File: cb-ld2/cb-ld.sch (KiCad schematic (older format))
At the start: 22 parts, among them P1 CONN_01X14, P2 CONN_01X14, U1 SKY13385, U2 MGA-81563, U3 MBC13916, U4 SKY13385

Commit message: Setting values for 433 MHz
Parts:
- removed C4: 3p, mysmd:SM0603S, symbol C
- added R?: 24, symbol R
- C3: value 10n -> 100n
- C5: value 1.5p -> 2.4p
- L2: value 10n -> 33n
- L3: value 10n -> 1u
- L4: value 6.8n -> 39n
- PS1: symbol PANSTAMP_NRG2 -> PANSTAMP_NRG2-RESCUE-cb-ld
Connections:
- wire segments 137 -> 136
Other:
- moved on the sheet: C5
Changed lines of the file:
@@
 EESchema Schematic File Version 2
+LIBS:cb-ld-rescue
 LIBS:power
 LIBS:device
@@
 encoding utf-8
 Sheet 1 1
-Title "cb-ld2"
+Title "cb-ld2 for 433 MHz applications"
 Date "2016-03-04"
 Rev "0.1"
@@
 $EndComp
 $Comp
-L PANSTAMP_NRG2 PS1
+L PANSTAMP_NRG2-RESCUE-cb-ld PS1
 U 1 1 54EE0213
 P 4850 4550
@@
 L C C5
 U 1 1 56D9BAD5
-P 9300 6250
-F 0 "C5" H 9350 6350 50  0000 L CNN
-F 1 "1.5p" H 9350 6150 50  0000 L CNN
-F 2 "mysmd:SM0603S" H 9300 6250 60  0001 C CNN
-F 3 "" H 9300 6250 60  0001 C CNN
-	1    9300 6250
+P 8900 6250
+F 0 "C5" H 8950 6350 50  0000 L CNN
+F 1 "2.4p" H 8950 6150 50  0000 L CNN
+F 2 "mysmd:SM0603S" H 8900 6250 60  0001 C CNN
+F 3 "" H 8900 6250 60  0001 C CNN
+	1    8900 6250
 	0    1    1    0
 $EndComp
-$Comp
-L C C4
-U 1 1 56D9BADC
-P 9050 6450
-F 0 "C4" H 9100 6550 50  0000 L CNN
-F 1 "3p" H 9100 6350 50  0000 L CNN
-F 2 "mysmd:SM0603S" H 9050 6450 60  0001 C CNN
-F 3 "" H 9050 6450 60  0001 C CNN
-	1    9050 6450
-	-1   0    0    1
-$EndComp
-Wire Wire Line
-	7700 6250 9150 6250
-Wire Wire Line
-	9050 6300 9050 6250
-Connection ~ 9050 6250
-$Comp
-L GND #PWR07
-U 1 1 56D9BAE6
-P 9050 6650
-F 0 "#PWR07" H 9050 6650 30  0001 C CNN
-F 1 "GND" H 9050 6580 30  0001 C CNN
-F 2 "" H 9050 6650 60  0001 C CNN
-F 3 "" H 9050 6650 60  0001 C CNN
-	1    9050 6650
-	-1   0    0    -1
-$EndComp
-Wire Wire Line
-	9050 6600 9050 6650
 $Comp
 L INDUCTOR_SMALL L2
@@
 P 9550 5800
 F 0 "L2" V 9504 5878 50  0000 L CNN
-F 1 "10n" V 9596 5878 50  0000 L CNN
+F 1 "33n" V 9596 5878 50  0000 L CNN
 F 2 "mysmd:SM0603S" H 9550 5800 50  0001 C CNN
 F 3 "" H 9550 5800 50  0000 C CNN
@@
 P 9050 5750
 F 0 "C3" H 9100 5850 50  0000 L CNN
-F 1 "10n" H 9100 5650 50  0000 L CNN
+F 1 "100n" H 9100 5650 50  0000 L CNN
 F 2 "mysmd:SM0603S" H 9050 5750 60  0001 C CNN
 F 3 "" H 9050 5750 60  0001 C CNN
@@
 P 11000 6250
 F 0 "L4" H 11000 6466 50  0000 C CNN
-F 1 "6.8n" H 11000 6374 50  0000 C CNN
+F 1 "39n" H 11000 6374 50  0000 C CNN
 F 2 "mysmd:SM0603S" H 11000 6250 50  0001 C CNN
 F 3 "" H 11000 6250 50  0000 C CNN
@@
 P 10350 3350
 F 0 "L3" V 10300 3200 50  0000 L CNN
-F 1 "10n" V 10400 3150 50  0000 L CNN
+F 1 "1u" V 10400 3150 50  0000 L CNN
 F 2 "mysmd:SM0603S" H 10350 3350 50  0001 C CNN
 F 3 "" H 10350 3350 50  0000 C CNN
@@
 Text Label 7050 6200 2    60   ~ 0
 RX_LNA
+$Comp
+L R R?
+U 1 1 57024CE4
+P 9300 6250
+F 0 "R?" V 9200 6250 50  0000 C CNN
+F 1 "24" V 9300 6250 50  0000 C CNN
+F 2 "" V 9230 6250 50  0000 C CNN
+F 3 "" H 9300 6250 50  0000 C CNN
+	1    9300 6250
+	0    1    1    0
+$EndComp
+Wire Wire Line
+	9150 6250 9050 6250
+Wire Wire Line
+	7700 6250 8750 6250
 $EndSCHEMATC

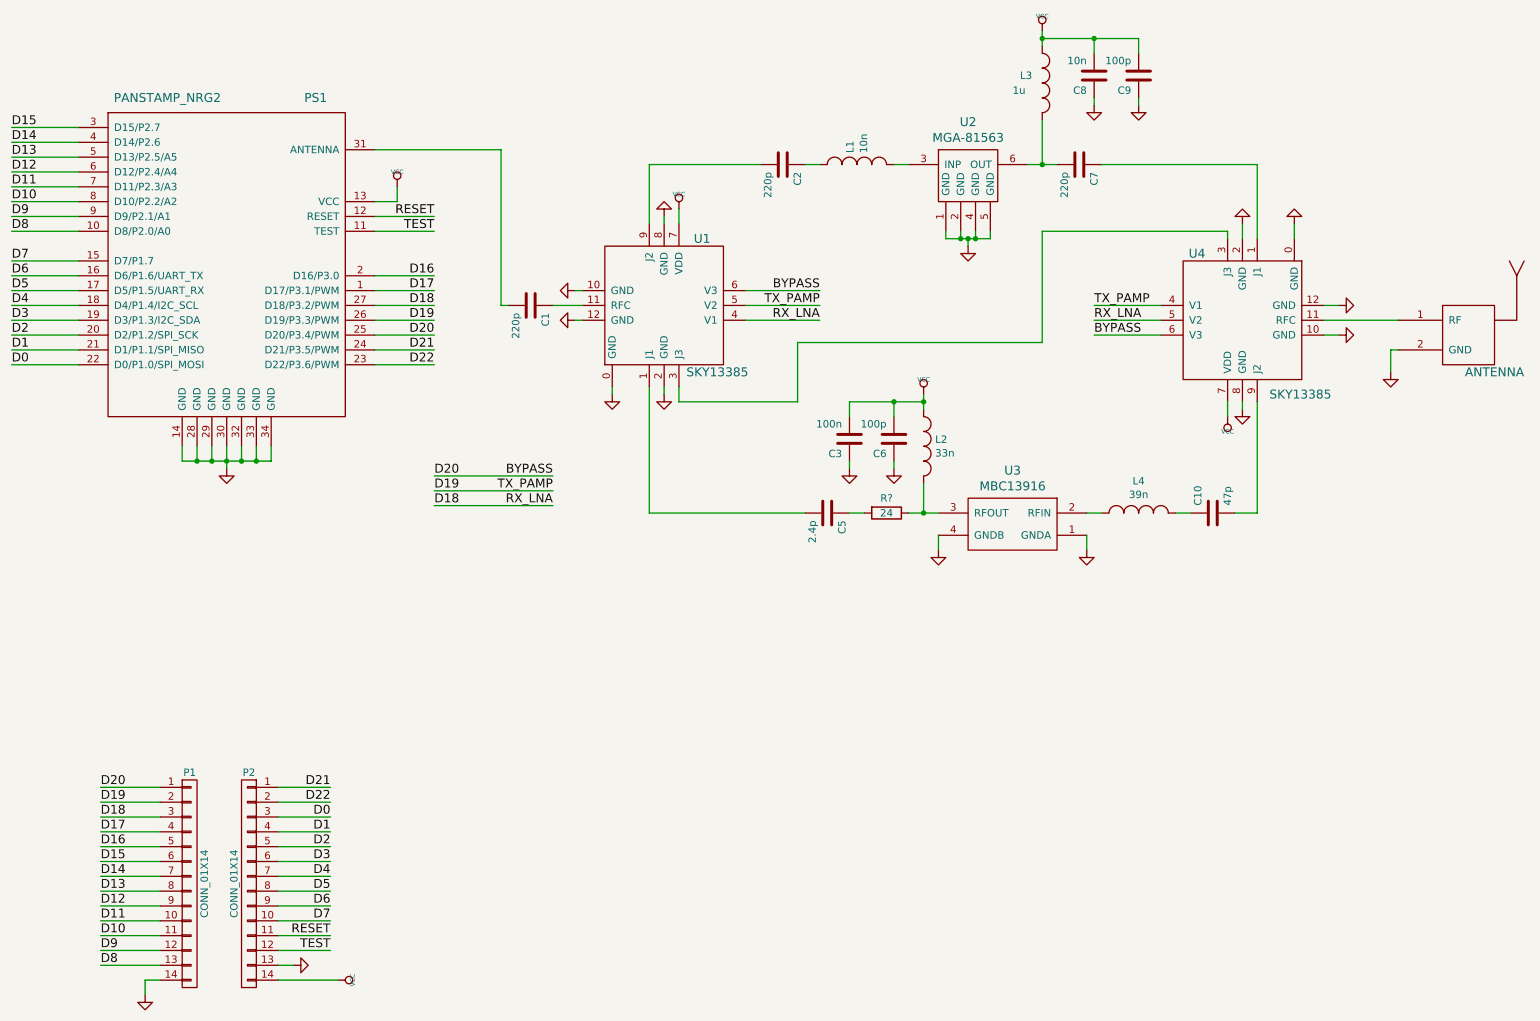
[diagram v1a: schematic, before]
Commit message: Natural evolution of the design after doing some tests
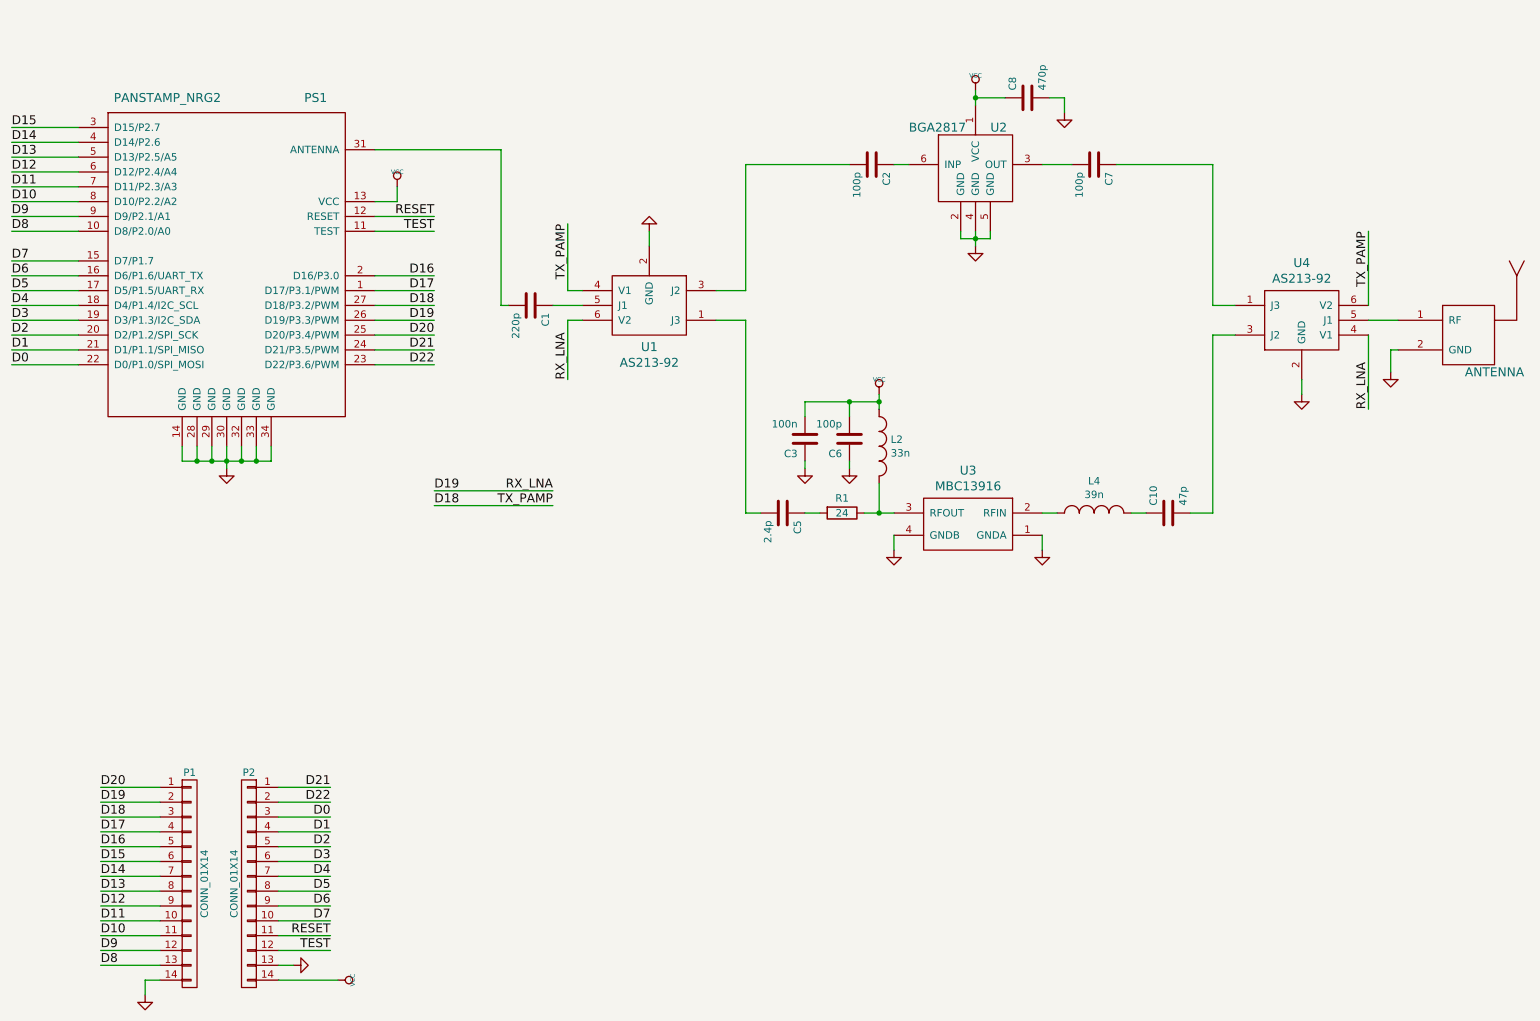
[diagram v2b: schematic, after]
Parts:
- removed C9: 100p, mysmd:SM0603S, symbol C
- removed L1: 10n, mysmd:SM0603S, symbol INDUCTOR_SMALL
- removed L3: 1u, mysmd:SM0603S, symbol INDUCTOR_SMALL
- removed U1, U4: SKY13385, mysmd:QFN12, symbol SKY13385
- removed U2: MGA-81563, mysmd:SC-70, symbol MGA-81563
- added U1, U4: AS213-92, mysmd:SC-70, symbol AS213-92
- added U2: BGA2817, mysmd:SC-70, symbol BGA2817
- C2, C7: value 220p -> 100p
- C8: value 10n -> 470p
- R1: renamed from R?; footprint (none) -> mysmd:SM0603S
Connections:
- net D18: now also U1.4 (V1), U4.6 (V2)
- net D19: now also U1.6 (V2), U4.4 (V1)
- net GND: now also C8.2, U1.2 (GND), U2.2 (GND), U2.4 (GND), U2.5 (GND), U4.2 (GND); no longer C8.1
- net VCC: now also C8.1, U2.1 (VCC); no longer C8.2
- net at ANT1.1 (RF): now also U4.5 (J1)
- net at C5.2: now also U1.1 (J3)
- net at C10.2: now also U4.3 (J2)
- net at C1.1: now also U1.5 (J1)
- net at C2.2: now also U1.3 (J2)
- net at C7.1: now also U4.1 (J3)
- net at C7.2: now also U2.3 (OUT)
- net at C2.1: now also U2.6 (INP)
- net BYPASS renamed D20
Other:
- moved on the sheet: C10, C2, C3, C5, C6, C7, C8, L2, L4, R1, U3

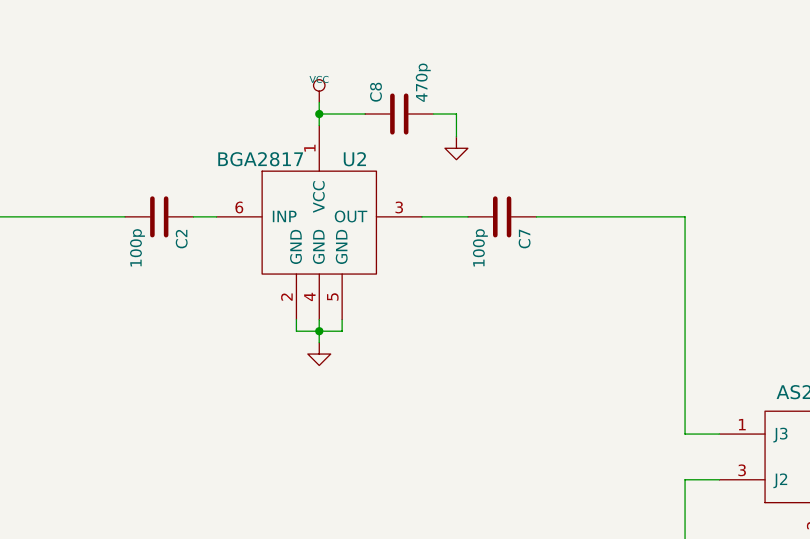
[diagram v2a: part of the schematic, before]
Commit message: PA replaced by MGA82563
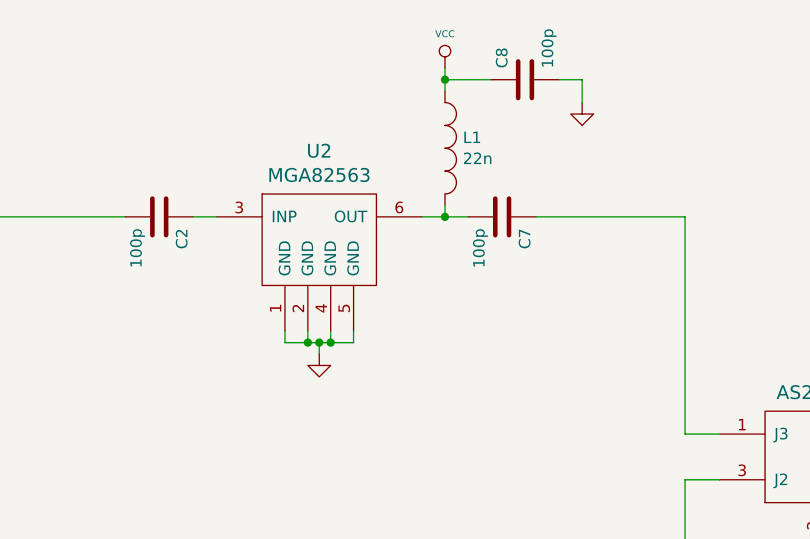
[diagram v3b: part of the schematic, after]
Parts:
- removed U2: BGA2817, mysmd:SC-70, symbol BGA2817
- added L1: 22n, mysmd:SM0603S, symbol INDUCTOR_SMALL
- added U2: MGA82563, mysmd:SC-70, symbol MGA82563
- C8: value 470p -> 100p
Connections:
- net GND: now also U2.1 (GND), U2.2 (GND), U2.4 (GND), U2.5 (GND)
- net VCC: now also L1.1
- net at C2.1: now also U2.3 (INP)
- net at C7.2: now also L1.2, U2.6 (OUT)
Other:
- moved on the sheet: C8
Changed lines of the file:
@@
 Title "cb-ld2 for 433 MHz applications"
 Date "2016-05-06"
-Rev "0.1"
+Rev "0.2"
 Comp "panStamp"
 Comment1 ""
@@
 L GND #PWR013
 U 1 1 56DA560D
-P 9900 4450
-F 0 "#PWR013" H 9900 4450 30  0001 C CNN
-F 1 "GND" H 9900 4380 30  0001 C CNN
-F 2 "" H 9900 4450 60  0001 C CNN
-F 3 "" H 9900 4450 60  0001 C CNN
-	1    9900 4450
-	1    0    0    -1
-$EndComp
-Wire Wire Line
-	9900 4350 9900 4450
-Connection ~ 9900 4400
-Wire Wire Line
-	9800 4350 9800 4400
+P 9900 4500
+F 0 "#PWR013" H 9900 4500 30  0001 C CNN
+F 1 "GND" H 9900 4430 30  0001 C CNN
+F 2 "" H 9900 4500 60  0001 C CNN
+F 3 "" H 9900 4500 60  0001 C CNN
+	1    9900 4500
+	1    0    0    -1
+$EndComp
 $Comp
 L C C7
@@
 L VCC #PWR014
 U 1 1 56DA5DCA
-P 9900 3400
-F 0 "#PWR014" H 9900 3500 30  0001 C CNN
-F 1 "VCC" H 9900 3500 30  0000 C CNN
-F 2 "" H 9900 3400 60  0001 C CNN
-F 3 "" H 9900 3400 60  0001 C CNN
-	1    9900 3400
+P 10450 3250
+F 0 "#PWR014" H 10450 3350 30  0001 C CNN
+F 1 "VCC" H 10450 3400 30  0000 C CNN
+F 2 "" H 10450 3250 60  0001 C CNN
+F 3 "" H 10450 3250 60  0001 C CNN
+	1    10450 3250
 	1    0    0    -1
 $EndComp
@@
 L C C8
 U 1 1 56DA6253
-P 10250 3450
-F 0 "C8" H 10300 3550 50  0000 L CNN
-F 1 "470p" H 10300 3350 50  0000 L CNN
-F 2 "mysmd:SM0603S" H 10250 3450 60  0001 C CNN
-F 3 "" H 10250 3450 60  0001 C CNN
-	1    10250 3450
+P 10800 3300
+F 0 "C8" H 10850 3400 50  0000 L CNN
+F 1 "100p" H 10850 3200 50  0000 L CNN
+F 2 "mysmd:SM0603S" H 10800 3300 60  0001 C CNN
+F 3 "" H 10800 3300 60  0001 C CNN
+	1    10800 3300
 	0    -1   -1   0
 $EndComp
@@
 L GND #PWR015
 U 1 1 56DA6263
-P 10500 3550
-F 0 "#PWR015" H 10500 3550 30  0001 C CNN
-F 1 "GND" H 10500 3480 30  0001 C CNN
-F 2 "" H 10500 3550 60  0001 C CNN
-F 3 "" H 10500 3550 60  0001 C CNN
-	1    10500 3550
+P 11050 3400
+F 0 "#PWR015" H 11050 3400 30  0001 C CNN
+F 1 "GND" H 11050 3330 30  0001 C CNN
+F 2 "" H 11050 3400 60  0001 C CNN
+F 3 "" H 11050 3400 60  0001 C CNN
+	1    11050 3400
 	-1   0    0    -1
 $EndComp
@@
 Wire Wire Line
 	12100 5450 12100 5350
-$Comp
-L BGA2817 U2
-U 1 1 572C5F7F
-P 9850 3950
-F 0 "U2" H 10000 4250 60  0000 L CNN
-F 1 "BGA2817" H 9450 4250 60  0000 L CNN
-F 2 "mysmd:SC-70" H 10000 4400 60  0001 C CNN
-F 3 "" H 10000 4400 60  0000 C CNN
-	1    9850 3950
-	1    0    0    -1
-$EndComp
 Wire Wire Line
 	11500 3900 10850 3900
 Wire Wire Line
-	9800 4400 10000 4400
-Wire Wire Line
-	10000 4400 10000 4350
-Wire Wire Line
 	10550 3900 10350 3900
 Wire Wire Line
-	9900 3400 9900 3500
-Wire Wire Line
-	10100 3450 9900 3450
-Connection ~ 9900 3450
-Wire Wire Line
-	10400 3450 10500 3450
-Wire Wire Line
-	10500 3450 10500 3550
+	10450 3250 10450 3350
+Wire Wire Line
+	10650 3300 10450 3300
+Connection ~ 10450 3300
+Wire Wire Line
+	10950 3300 11050 3300
+Wire Wire Line
+	11050 3300 11050 3400
+$Comp
+L MGA82563 U2
+U 1 1 576D24BC
+P 9850 4000
+F 0 "U2" H 9900 4387 60  0000 C CNN
+F 1 "MGA82563" H 9900 4281 60  0000 C CNN
+F 2 "mysmd:SC-70" H 10000 4450 60  0001 C CNN
+F 3 "" H 10000 4450 60  0000 C CNN
+	1    9850 4000
+	1    0    0    -1
+$EndComp
+Wire Wire Line
+	9750 4400 9750 4450
+Wire Wire Line
+	9750 4450 10050 4450
+Wire Wire Line
+	10050 4450 10050 4400
+Wire Wire Line
+	9950 4400 9950 4450
+Connection ~ 9950 4450
+Wire Wire Line
+	9850 4400 9850 4450
+Connection ~ 9850 4450
+Wire Wire Line
+	9900 4500 9900 4450
+Connection ~ 9900 4450
+$Comp
+L INDUCTOR_SMALL L1
+U 1 1 576D2A60
+P 10450 3600
+F 0 "L1" V 10404 3678 50  0000 L CNN
+F 1 "22n" V 10496 3678 50  0000 L CNN
+F 2 "mysmd:SM0603S" H 10450 3600 50  0001 C CNN
+F 3 "" H 10450 3600 50  0000 C CNN
+	1    10450 3600
+	0    1    1    0
+$EndComp
+Wire Wire Line
+	10450 3850 10450 3900
+Connection ~ 10450 3900
 $EndSCHEMATC

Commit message: Preparing board for 900 MHz
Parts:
- added C4: 3p, mysmd:SM0603S, symbol C
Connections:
- net GND: now also C4.1
- net at C5.2, U1.1 (J3): now also C4.2
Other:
- note added: "0 (900MHz)"
- note added: "1.5p (900MHz)"
- note added: "10n (900MHz)"
- note added: "900MHz"
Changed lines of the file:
@@
 LIBS:contrib
 LIBS:valves
-LIBS:atmega8
-LIBS:atmel89cxxxx
-LIBS:atmel-1
-LIBS:atmel-2005
-LIBS:avr
-LIBS:avr-1
-LIBS:avr-2
-LIBS:avr-3
-LIBS:avr-4
-LIBS:hopf
-LIBS:rfm-ash
-LIBS:mycomponents
 LIBS:cb-ld-cache
 EELAYER 25 0
@@
 Title "cb-ld2 for 433 MHz applications"
 Date "2016-05-06"
-Rev "0.2"
+Rev "1.0"
 Comp "panStamp"
 Comment1 ""
@@
 U 1 1 56D9BAD5
 P 8600 6250
-F 0 "C5" H 8650 6350 50  0000 L CNN
-F 1 "2.4p" H 8650 6150 50  0000 L CNN
+F 0 "C5" H 8450 6350 50  0000 L CNN
+F 1 "2.4p" H 8400 6150 50  0000 L CNN
 F 2 "mysmd:SM0603S" H 8600 6250 60  0001 C CNN
 F 3 "" H 8600 6250 60  0001 C CNN
@@
 	8150 4950 8350 4950
 Wire Wire Line
-	8350 4950 8350 6250
+	8350 4950 8350 6450
 Wire Wire Line
 	8150 4750 8350 4750
@@
 	10450 3850 10450 3900
 Connection ~ 10450 3900
+$Comp
+L C C4
+U 1 1 57C3FDC5
+P 8350 6600
+F 0 "C4" H 8400 6700 50  0000 L CNN
+F 1 "3p" H 8400 6500 50  0000 L CNN
+F 2 "mysmd:SM0603S" H 8350 6600 60  0001 C CNN
+F 3 "" H 8350 6600 60  0001 C CNN
+	1    8350 6600
+	-1   0    0    1
+$EndComp
+Connection ~ 8350 6250
+$Comp
+L GND #PWR017
+U 1 1 57C3FF57
+P 8350 6850
+F 0 "#PWR017" H 8350 6850 30  0001 C CNN
+F 1 "GND" H 8350 6780 30  0001 C CNN
+F 2 "" H 8350 6850 60  0001 C CNN
+F 3 "" H 8350 6850 60  0001 C CNN
+	1    8350 6850
+	-1   0    0    -1
+$EndComp
+Wire Wire Line
+	8350 6850 8350 6750
+Text Notes 7550 6000 0    60   ~ 0
+1.5p (900MHz)
+Wire Notes Line
+	8150 6350 8150 7050
+Wire Notes Line
+	8250 5950 8600 5950
+Wire Notes Line
+	8600 5950 8600 6150
+Wire Notes Line
+	8150 6350 8550 6350
+Wire Notes Line
+	8550 6350 8550 7050
+Wire Notes Line
+	8550 7050 8150 7050
+Text Notes 8200 7150 0    60   ~ 0
+900MHz
+Text Notes 9050 6850 1    60   ~ 0
+0 (900MHz)
+Text Notes 9300 5650 0    60   ~ 0
+10n (900MHz)
 $EndSCHEMATC
